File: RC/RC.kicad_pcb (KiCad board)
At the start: 2 copper layers, 120 x 100 mm, 45 parts, among them J1 BEC, J10 CJVL53L0XV2, J11 CJMCU-20948, J12 A3144 REMOTE, J2 ESP32L, J3 ESP32R, J4 BuckIn-, J5 BuckIn+, J6 BuckOut-, J7 BuckOut+, J8 VBAT_SENSE_IN, J9 3V3 LINK, M1 MG90

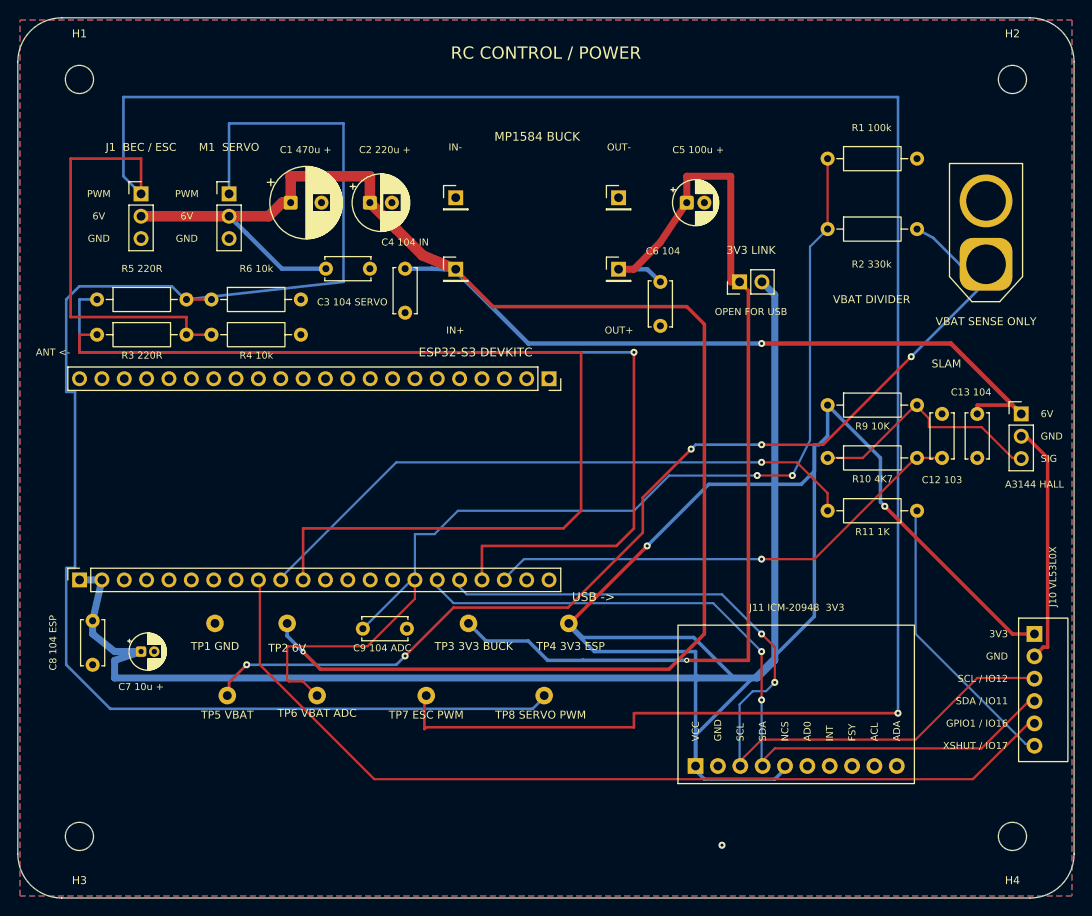
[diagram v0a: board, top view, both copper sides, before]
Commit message: Optimize RC PCB outline and production labeling
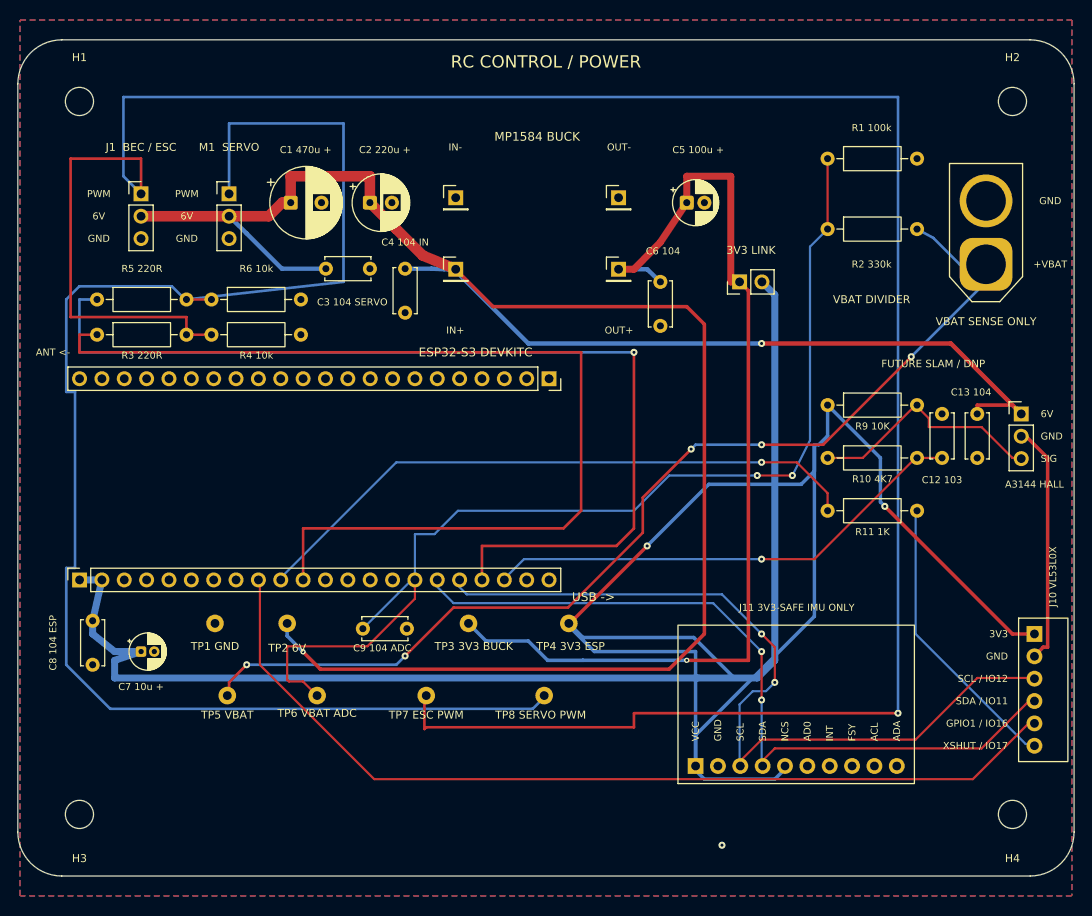
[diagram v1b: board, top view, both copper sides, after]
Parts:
- moved H1 2.50 mm to (27.0, 89.5)
- moved H2 2.50 mm to (133.0, 89.5)
- moved H3 2.50 mm to (27.0, 170.5)
- moved H4 2.50 mm to (133.0, 170.5)
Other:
- board size 120 x 100 mm -> 120 x 95 mm
- board text added: "+VBAT"
- board text added: "FUTURE SLAM / DNP"
- board text added: "J11 3V3-SAFE IMU ONLY"
- board text removed: "J11 ICM-20948 3V3"
- board text removed: "OPEN FOR USB"
- board text removed: "SLAM"
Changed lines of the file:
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@@
 	(footprint "MountingHole:MountingHole_3.2mm_M3"
 		(layer "F.Cu")
-		(at 27 87)
+		(at 27 89.5)
 		(property "Reference" "H1"
 			(at 0 -2.5 0)
@@
 	(footprint "MountingHole:MountingHole_3.2mm_M3"
 		(layer "F.Cu")
-		(at 27 173)
+		(at 27 170.5)
 		(property "Reference" "H3"
 			(at 0 -2.5 0)
@@
 	(footprint "MountingHole:MountingHole_3.2mm_M3"
 		(layer "F.Cu")
-		(at 133 173)
+		(at 133 170.5)
 		(property "Reference" "H4"
 			(at 0 -2.5 0)
@@
 	(footprint "MountingHole:MountingHole_3.2mm_M3"
 		(layer "F.Cu")
-		(at 133 87)
+		(at 133 89.5)
 		(property "Reference" "H2"
 			(at 0 -2.5 0)
@@
 	)
 	(gr_arc
-		(start 20 85)
-		(mid 21.464466 81.464466)
-		(end 25 80)
+		(start 20 87.5)
+		(mid 21.464466 83.964466)
+		(end 25 82.5)
 		(stroke
 			(width 0.05)
@@
 	)
 	(gr_line
-		(start 20 175)
-		(end 20 85)
+		(start 20 172.5)
+		(end 20 87.5)
 		(stroke
 			(width 0.05)
@@
 	)
 	(gr_line
-		(start 25 80)
-		(end 135 80)
+		(start 25 82.5)
+		(end 135 82.5)
 		(stroke
 			(width 0.05)
@@
 	)
 	(gr_arc
-		(start 25 180)
-		(mid 21.464466 178.535533)
-		(end 20 175)
+		(start 25 177.5)
+		(mid 21.464466 176.035533)
+		(end 20 172.5)
 		(stroke
 			(width 0.05)
@@
 	)
 	(gr_arc
-		(start 135 80)
-		(mid 138.535533 81.464466)
-		(end 140 85)
+		(start 135 82.5)
+		(mid 138.535533 83.964466)
+		(end 140 87.5)
 		(stroke
 			(width 0.05)
@@
 	)
 	(gr_line
-		(start 135 180)
-		(end 25 180)
+		(start 135 177.5)
+		(end 25 177.5)
 		(stroke
 			(width 0.05)
@@
 	)
 	(gr_line
-		(start 140 85)
-		(end 140 175)
+		(start 140 87.5)
+		(end 140 172.5)
 		(stroke
 			(width 0.05)
@@
 	)
 	(gr_arc
-		(start 140 175)
-		(mid 138.535533 178.535533)
-		(end 135 180)
+		(start 140 172.5)
+		(mid 138.535533 176.035533)
+		(end 135 177.5)
 		(stroke
 			(width 0.05)
@@
 		)
 	)
-	(gr_text "OPEN FOR USB"
-		(at 103.3 113.4 0)
-		(layer "F.SilkS")
-		(effects
-			(font
-				(size 0.8 0.8)
-				(thickness 0.13)
-			)
-		)
-	)
-	(gr_text "J11 ICM-20948  3V3"
+	(gr_text "J11 3V3-SAFE IMU ONLY"
 		(at 108.5 147 0)
 		(layer "F.SilkS")
@@
 		)
 	)
+	(gr_text "GND"
+		(at 137.3 100.8 0)
+		(layer "F.SilkS")
+		(effects
+			(font
+				(size 0.8 0.8)
+				(thickness 0.13)
+			)
+		)
+	)
+	(gr_text "+VBAT"
+		(at 137.3 108 0)
+		(layer "F.SilkS")
+		(effects
+			(font
+				(size 0.8 0.8)
+				(thickness 0.13)
+			)
+		)
+	)
 	(gr_text "C8 104 ESP"
 		(at 24 151 90)
@@
 		)
 	)
+	(gr_text "FUTURE SLAM / DNP"
+		(at 124 119.3 0)
+		(layer "F.SilkS")
+		(effects
+			(font
+				(size 0.85 0.85)
+				(thickness 0.13)
+			)
+		)
+	)
 	(gr_text "H1"
-		(at 27 81.8 0)
+		(at 27 84.5 0)
 		(layer "F.SilkS")
 		(effects
@@
 	)
 	(gr_text "H3"
-		(at 27 178 0)
+		(at 27 175.5 0)
 		(layer "F.SilkS")
 		(effects
@@
 	)
 	(gr_text "H2"
-		(at 133 81.8 0)
+		(at 133 84.5 0)
 		(layer "F.SilkS")
 		(effects
@@
 	)
 	(gr_text "H4"
-		(at 133 178 0)
+		(at 133 175.5 0)
 		(layer "F.SilkS")
 		(effects
@@
 		)
 	)
-	(gr_text "SLAM"
-		(at 125.5 119.3 0)
-		(layer "F.SilkS")
-		(effects
-			(font
-				(size 0.9 0.9)
-				(thickness 0.144)
-			)
-		)
-	)
 	(gr_text "ESP32-S3 DEVKITC"
 		(at 72 118 0)
@@
 	)
 	(gr_text "RC CONTROL / POWER"
-		(at 80 84 0)
+		(at 80 85 0)
 		(layer "F.SilkS")
 		(effects
@@
 		(polygon
 			(pts
-				(xy 129 169) (xy 137 169) (xy 137 177) (xy 129 177)
+				(xy 129 166.5) (xy 137 166.5) (xy 137 174.5) (xy 129 174.5)
 			)
 		)
@@
 		(polygon
 			(pts
-				(xy 23 169) (xy 31 169) (xy 31 177) (xy 23 177)
+				(xy 23 166.5) (xy 31 166.5) (xy 31 174.5) (xy 23 174.5)
 			)
 		)
@@
 		(polygon
 			(pts
-				(xy 23 83) (xy 31 83) (xy 31 91) (xy 23 91)
+				(xy 23 85.5) (xy 31 85.5) (xy 31 93.5) (xy 23 93.5)
 			)
 		)
@@
 		(polygon
 			(pts
-				(xy 129 83) (xy 137 83) (xy 137 91) (xy 129 91)
+				(xy 129 85.5) (xy 137 85.5) (xy 137 93.5) (xy 129 93.5)
 			)
 		)

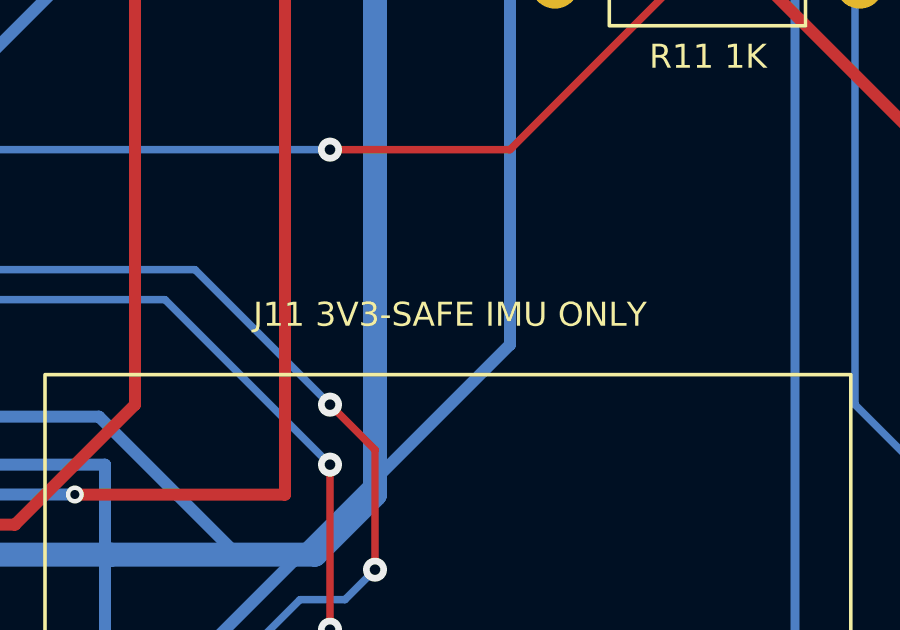
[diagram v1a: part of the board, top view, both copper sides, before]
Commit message: Prepare RC PCB for manufacturing
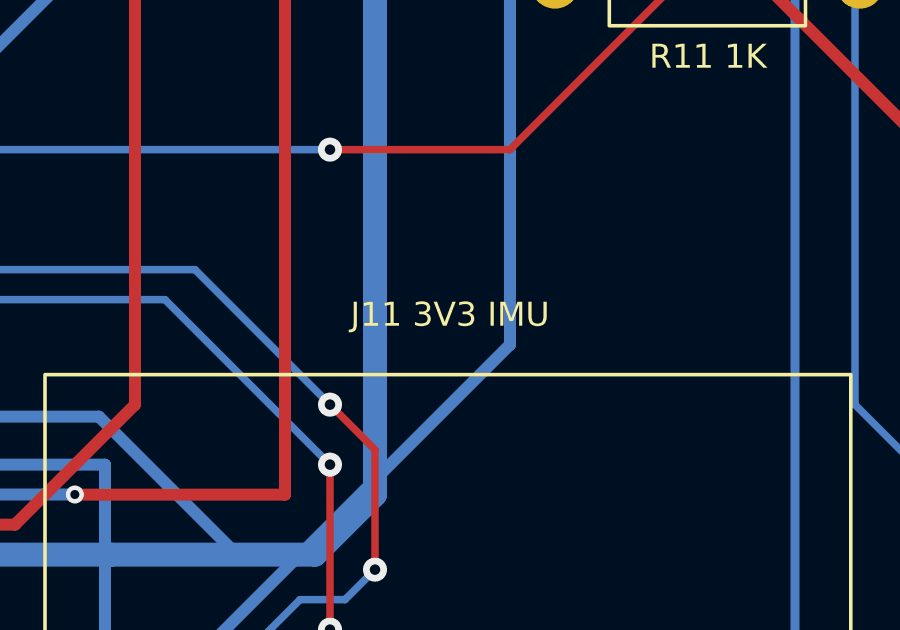
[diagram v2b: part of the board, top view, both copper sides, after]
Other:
- board text added: "J11 3V3 IMU"
- board text removed: "J11 3V3-SAFE IMU ONLY"
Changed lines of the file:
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@@
 		)
 	)
-	(gr_text "J11 3V3-SAFE IMU ONLY"
+	(gr_text "J11 3V3 IMU "
 		(at 108.5 147 0)
 		(layer "F.SilkS")

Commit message: Release RC carrier PCB v1.0 for fabrication
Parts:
- moved C12 96.9 mm to (35.0, 94.0), turned to 0 degrees
- moved C13 84.9 mm to (50.0, 94.0), turned to 180 degrees
- moved R9 84.6 mm to (35.0, 89.0)
- moved J12 82.1 mm to (58.0, 94.0), turned to 90 degrees
- moved R10 76.0 mm to (48.0, 89.0)
- moved R1 71.1 mm to (67.0, 151.0), turned to -90 degrees
- moved R11 69.4 mm to (61.0, 89.0)
- moved R2 62.4 mm to (71.0, 151.0), turned to -90 degrees
- moved H2 27.6 mm to (105.5, 92.0)
- moved H4 27.6 mm to (105.5, 168.0)
- moved J10 27.1 mm to (108.5, 148.2)
- moved TP4 21.8 mm to (62.0, 156.0)
- moved J11 21.6 mm to (75.5, 166.5)
- moved J8 21.1 mm to (109.0, 110.0)
- moved TP8 19.9 mm to (62.0, 166.0)
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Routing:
- net +3.3V: track 327.7 -> 516.1 mm, vias 2 -> 7
- net /PWM_ESC_OUT: track 277.2 -> 111.0 mm, vias 1 -> 0
- net +6V: track 260.5 -> 184.8 mm, vias 2 -> 4
- net /VBAT_SENSE: track 123.2 -> 48.4 mm, vias 2 -> 0
- net /PWM_ESC: track 117.3 -> 49.9 mm, vias 0 -> 2
- net /VL_XSHUT: track 33.0 -> 89.4 mm
- net /PWM_SERVO_OUT: track 175.6 -> 120.4 mm, vias 0 -> 3
- net /IO14: track 55.9 -> 100.2 mm, vias 1 -> 0
- net /IO16: track 106.0 -> 68.5 mm
- net /IO12: track 93.8 -> 60.4 mm, vias 2 -> 0
- net /PWM_SERVO: track 113.0 -> 81.2 mm
- net /IO11: track 88.6 -> 58.7 mm, vias 2 -> 0
- net GND: track 27.5 -> 5.15 mm, vias 1 -> 0
- net /VBAT: track 120.2 -> 103.4 mm, vias 5 -> 3
- net /IO17: track 71.5 -> 83.4 mm, vias 1 -> 0
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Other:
- board size 120 x 95 mm -> 95 x 90 mm
- board text added: "3V3"
- board text added: "C1 470u+"
- board text added: "C2 220u+"
- board text added: "C5 100u+"
- board text added: "C7 10u+"
- board text added: "C8 104"
- board text added: "ESP32-S3 / 25.4mm"
- board text added: "GP1"
- board text added: "GP1=IO16 XSH=IO17"
- board text added: "J1 ESC"
- board text added: "J10 VL53L0X"
- board text added: "J10: SCL=IO12 SDA=IO11"
- board text added: "J11 3V3-SAFE IMU / DNP"
- board text added: "J12 HALL"
- board text added: "MP1584"
- board text added: "R4 10K"
- board text added: "R6 10K"
- board text added: "RC CONTROL"
- board text added: "REMOVE FOR USB"
- board text added: "SCL"
- board text added: "SDA"
- board text added: "SIG GND 6V"
- board text added: "SLAM / DNP"
- board text added: "TP3 3V3R"
- board text added: "TP4 3V3"
- board text added: "TP6 ADC"
- board text added: "TP7 ESC"
- board text added: "TP8 SERVO"
- board text added: "USB CLEAR ->"
- board text added: "VBAT DIV"
- board text added: "XSH"
- board text removed: "+VBAT"
- board text removed: "6V"
- board text removed: "A3144 HALL"
- board text removed: "C1 470u +"
- board text removed: "C2 220u +"
- board text removed: "C3 104 SERVO"
- board text removed: "C4 104 IN"
- board text removed: "C5 100u +"
- board text removed: "C6 104"
- board text removed: "C7 10u +"
- board text removed: "C8 104 ESP"
- board text removed: "ESP32-S3 DEVKITC"
- board text removed: "FUTURE SLAM / DNP"
- board text removed: "J1 BEC / ESC"
- board text removed: "J11 3V3 IMU"
- board text removed: "MP1584 BUCK"
- board text removed: "PWM"
- board text removed: "R1 100k"
- board text removed: "R2 330k"
- board text removed: "R4 10k"
- board text removed: "R6 10k"
- board text removed: "RC CONTROL / POWER"
- board text removed: "SIG"
- board text removed: "TP3 3V3 BUCK"
- board text removed: "TP4 3V3 ESP"
- board text removed: "TP6 VBAT ADC"
- board text removed: "TP7 ESC PWM"
- board text removed: "TP8 SERVO PWM"
- board text removed: "USB ->"
- board text removed: "VBAT DIVIDER"

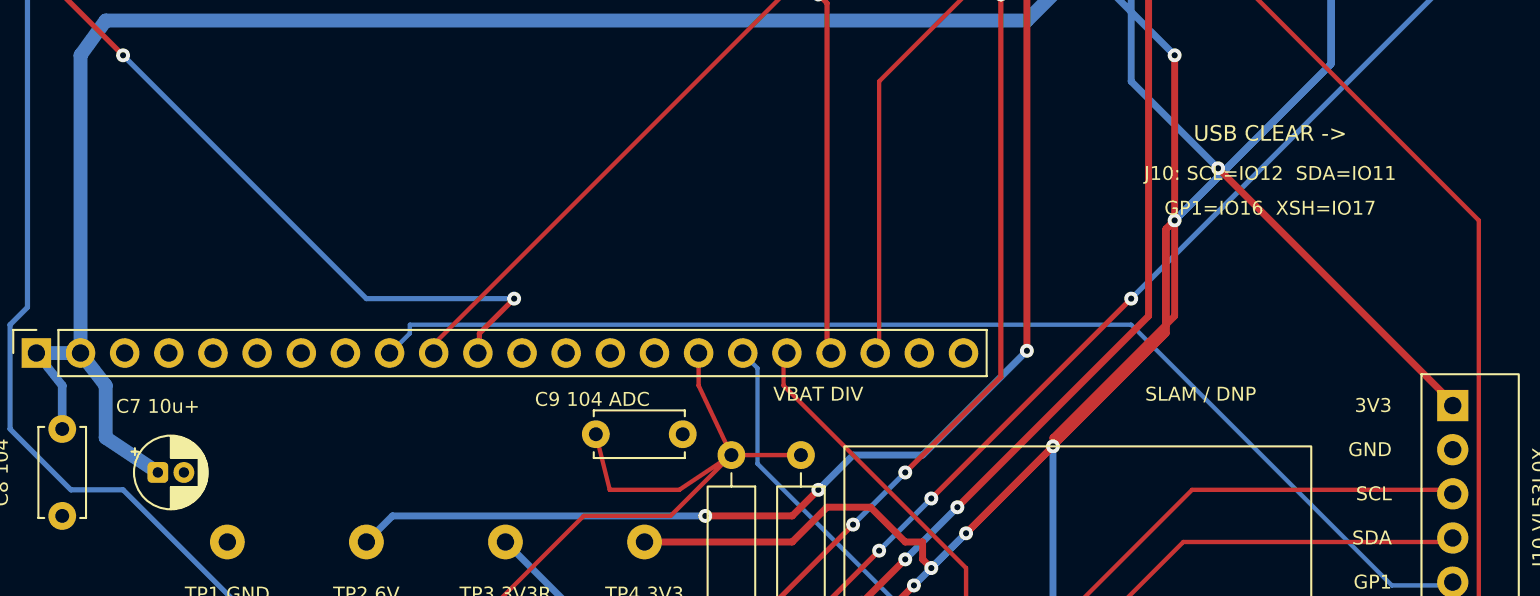
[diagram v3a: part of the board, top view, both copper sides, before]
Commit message: Archive validated RC PCB before aggressive compaction
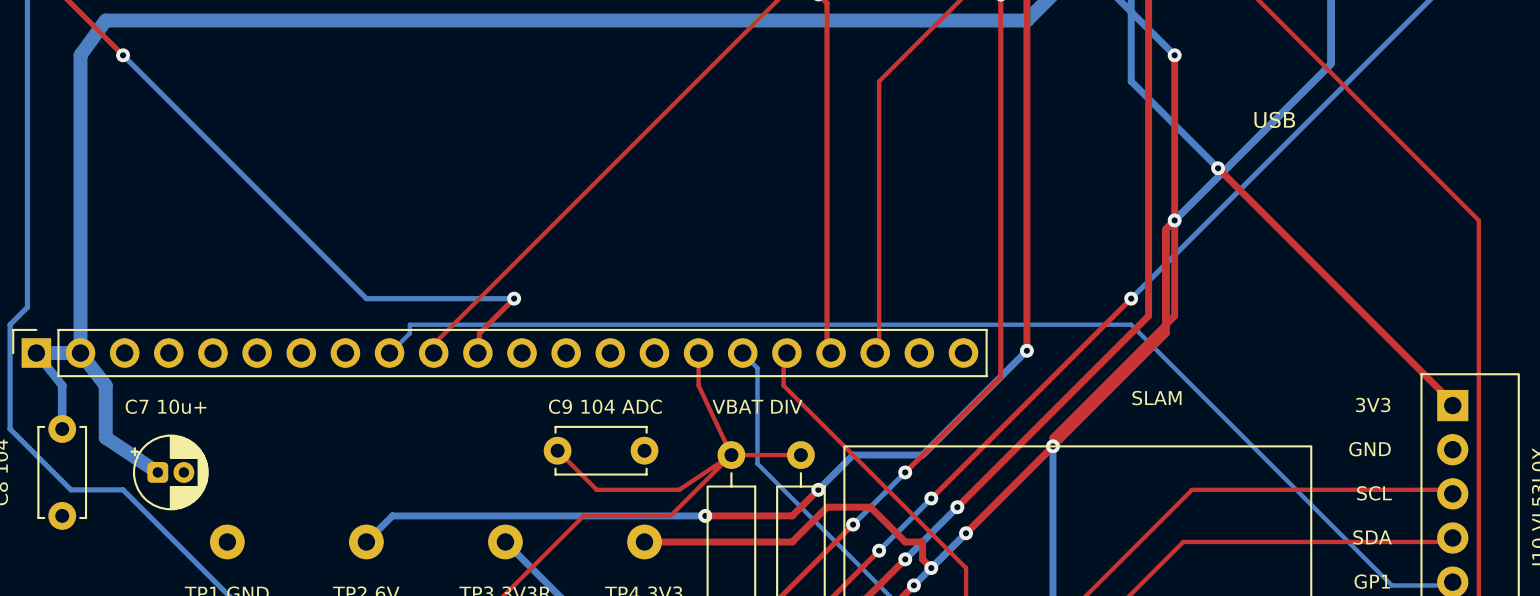
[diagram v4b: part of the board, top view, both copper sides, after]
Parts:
- moved C9 2.40 mm to (57.0, 150.8)
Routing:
- net /VBAT_SENSE: track 48.4 -> 49.0 mm
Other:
- board text added: "SLAM"
- board text added: "USB"
- board text removed: "GP1=IO16 XSH=IO17"
- board text removed: "J10: SCL=IO12 SDA=IO11"
- board text removed: "SLAM / DNP"
- board text removed: "USB CLEAR ->"
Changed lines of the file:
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@@
 	(footprint "Capacitor_THT:C_Disc_D5.0mm_W2.5mm_P5.00mm"
 		(layer "F.Cu")
-		(at 59.2 149.8)
+		(at 57 150.75)
 		(descr "C, Disc series, Radial, pin pitch=5.00mm, diameter*width=5*2.5mm^2, Capacitor, http://cdn-reichelt.de/documents/datenblatt/B300/DS_KERKO_TC.pdf")
 		(tags "C Disc series Radial pin pitch 5.00mm diameter 5mm width 2.5mm Capacitor")
@@
 		)
 	)
-	(gr_text "C7 10u+"
-		(at 34 148.2 0)
+	(gr_text "R5 220R"
+		(at 34.1 107.8 0)
 		(layer "F.SilkS")
 		(effects
@@
 		)
 	)
-	(gr_text "R5 220R"
-		(at 34.1 107.8 0)
+	(gr_text "R3 220R"
+		(at 34.1 117 0)
 		(layer "F.SilkS")
 		(effects
@@
 		)
 	)
-	(gr_text "R3 220R"
-		(at 34.1 117 0)
+	(gr_text "C7 10u+"
+		(at 34.5 148.25 0)
 		(layer "F.SilkS")
 		(effects
@@
 	)
 	(gr_text "C9 104 ADC"
-		(at 59 147.8 0)
+		(at 59.75 148.25 0)
 		(layer "F.SilkS")
 		(effects
@@
 		)
 	)
-	(gr_text "IN-"
-		(at 69.75 97 0)
+	(gr_text "VBAT DIV"
+		(at 68.5 148.25 0)
 		(layer "F.SilkS")
 		(effects
@@
 		)
 	)
-	(gr_text "IN+"
-		(at 69.75 112.4 0)
+	(gr_text "IN-"
+		(at 69.75 97 0)
 		(layer "F.SilkS")
 		(effects
@@
 		)
 	)
-	(gr_text "VBAT DIV"
-		(at 72 147.5 0)
+	(gr_text "IN+"
+		(at 69.75 112.4 0)
 		(layer "F.SilkS")
 		(effects
@@
 		)
 	)
-	(gr_text "SLAM / DNP"
-		(at 94 147.5 0)
+	(gr_text "SLAM\n"
+		(at 91.5 147.75 0)
 		(layer "F.SilkS")
 		(effects
@@
 		)
 	)
-	(gr_text "J10: SCL=IO12  SDA=IO11"
-		(at 98 134.8 0)
-		(layer "F.SilkS")
-		(effects
-			(font
-				(size 0.8 0.8)
-				(thickness 0.13)
-			)
-		)
-	)
-	(gr_text "GP1=IO16  XSH=IO17"
-		(at 98 136.8 0)
-		(layer "F.SilkS")
-		(effects
-			(font
-				(size 0.8 0.8)
-				(thickness 0.13)
-			)
-		)
-	)
 	(gr_text "3V3 LINK"
 		(at 99 106 0)
@@
 		)
 	)
-	(gr_text "USB CLEAR ->"
-		(at 98 132.5 0)
+	(gr_text "USB\n"
+		(at 98.25 131.75 0)
 		(layer "F.SilkS")
 		(effects
@@
 	)
 	(segment
-		(start 67 151)
-		(end 71 151)
+		(start 64 153)
+		(end 59.25 153)
 		(width 0.25)
 		(layer "F.Cu")
@@
 	)
 	(segment
-		(start 65.113 147)
-		(end 65.113 145.13)
+		(start 67 151)
+		(end 71 151)
 		(width 0.25)
 		(layer "F.Cu")
@@
 	)
 	(segment
-		(start 47 166)
-		(end 46 166)
+		(start 65.113 147)
+		(end 65.113 145.13)
 		(width 0.25)
 		(layer "F.Cu")
@@
 	)
 	(segment
-		(start 60 153)
-		(end 59.2 149.8)
+		(start 47 166)
+		(end 46 166)
 		(width 0.25)
 		(layer "F.Cu")
@@
 	)
 	(segment
-		(start 63.5 154.5)
-		(end 58.5 154.5)
+		(start 59.25 153)
+		(end 57 150.75)
 		(width 0.25)
 		(layer "F.Cu")
@@
 	)
 	(segment
-		(start 58.5 154.5)
-		(end 47 166)
+		(start 63.5 154.5)
+		(end 58.5 154.5)
 		(width 0.25)
 		(layer "F.Cu")
@@
 	)
 	(segment
-		(start 64 153)
-		(end 60 153)
+		(start 58.5 154.5)
+		(end 47 166)
 		(width 0.25)
 		(layer "F.Cu")
